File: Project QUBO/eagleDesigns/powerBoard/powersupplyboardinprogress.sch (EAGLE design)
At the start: 8 parts

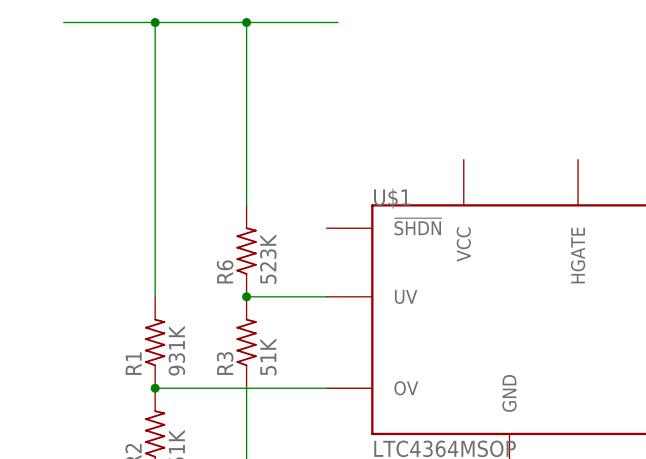
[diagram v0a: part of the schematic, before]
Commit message: Added supporting components for the SHDN pin to the schematic and part's list
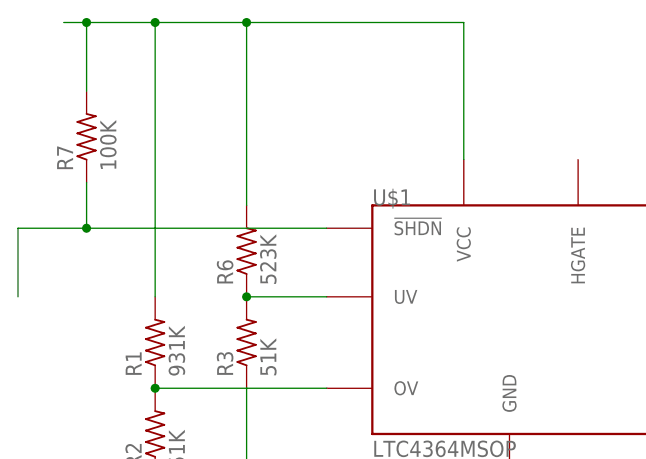
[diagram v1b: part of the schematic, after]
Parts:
- added R7: 100K, resistor:R-US_R0805
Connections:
- new net N$1: R7.1, U$1.!SHDN!
- net N$7: now also R7.2, U$1.VCC
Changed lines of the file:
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@@
 <part name="R3" library="resistor" deviceset="R-US_" device="M0805" value="51K"/>
 <part name="R6" library="resistor" deviceset="R-US_" device="M0805" value="523K"/>
+<part name="R7" library="resistor" deviceset="R-US_" device="R0805" value="100K"/>
 </parts>
 <sheets>
@@
 <instance part="R3" gate="G$1" x="27.94" y="73.66" rot="R90"/>
 <instance part="R6" gate="G$1" x="27.94" y="83.82" rot="R90"/>
+<instance part="R7" gate="G$1" x="10.16" y="96.52" rot="R90"/>
 </instances>
 <busses>
@@
 <net name="N$7" class="0">
 <segment>
-<wire x1="27.94" y1="109.22" x2="38.1" y2="109.22" width="0.1524" layer="91"/>
 <pinref part="R6" gate="G$1" pin="2"/>
 <wire x1="27.94" y1="88.9" x2="27.94" y2="109.22" width="0.1524" layer="91"/>
@@
 <wire x1="17.78" y1="109.22" x2="27.94" y2="109.22" width="0.1524" layer="91"/>
 <junction x="27.94" y="109.22"/>
-<wire x1="7.62" y1="109.22" x2="17.78" y2="109.22" width="0.1524" layer="91"/>
+<wire x1="7.62" y1="109.22" x2="10.16" y2="109.22" width="0.1524" layer="91"/>
 <junction x="17.78" y="109.22"/>
+<pinref part="U$1" gate="G$1" pin="VCC"/>
+<wire x1="10.16" y1="109.22" x2="17.78" y2="109.22" width="0.1524" layer="91"/>
+<wire x1="27.94" y1="109.22" x2="52.07" y2="109.22" width="0.1524" layer="91"/>
+<wire x1="52.07" y1="109.22" x2="52.07" y2="93.98" width="0.1524" layer="91"/>
+<pinref part="R7" gate="G$1" pin="2"/>
+<wire x1="10.16" y1="109.22" x2="10.16" y2="101.6" width="0.1524" layer="91"/>
+<junction x="10.16" y="109.22"/>
 </segment>
 </net>
+<net name="N$1" class="0">
+<segment>
+<pinref part="R7" gate="G$1" pin="1"/>
+<wire x1="10.16" y1="91.44" x2="10.16" y2="86.36" width="0.1524" layer="91"/>
+<pinref part="U$1" gate="G$1" pin="!SHDN!"/>
+<wire x1="10.16" y1="86.36" x2="36.83" y2="86.36" width="0.1524" layer="91"/>
+<wire x1="10.16" y1="86.36" x2="2.54" y2="86.36" width="0.1524" layer="91"/>
+<wire x1="2.54" y1="86.36" x2="2.54" y2="78.74" width="0.1524" layer="91"/>
+<junction x="10.16" y="86.36"/>
+</segment>
+</net>

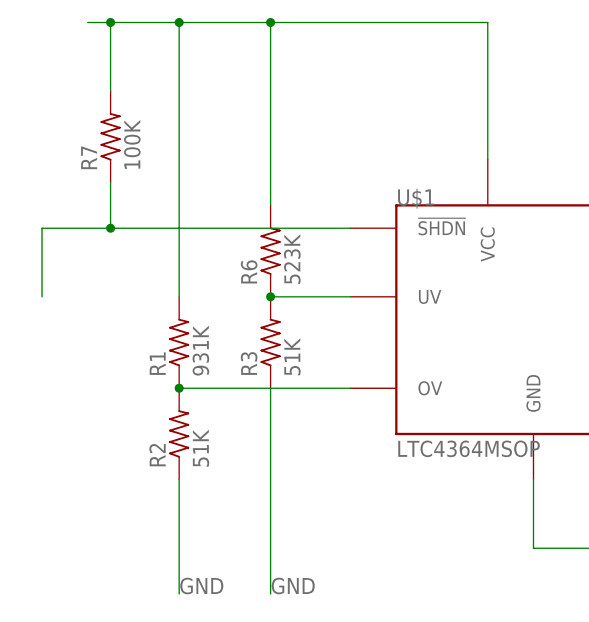
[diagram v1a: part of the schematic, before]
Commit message: 
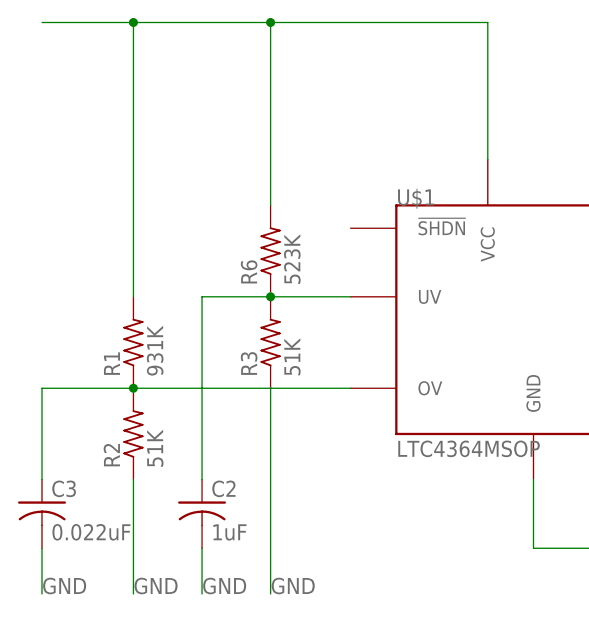
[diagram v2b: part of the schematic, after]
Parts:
- removed R7: 100K, resistor:R-US_R0805
- added C2: 1uF, resistor:C-USC0805
- added C3: 0.022uF, resistor:C-USC0805
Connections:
- removed net N$1: R7.1, U$1.!SHDN!
- net GND: now also C2.2, C3.2
- net N$5: now also C2.1
- net N$6: now also C3.1
- net N$7: no longer R7.2
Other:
- moved on the sheet: R1, R2
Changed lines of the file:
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@@
 <?xml version="1.0" encoding="utf-8"?>
 <!DOCTYPE eagle SYSTEM "eagle.dtd">
-<eagle version="8.3.2">
+<eagle version="8.4.0">
 <drawing>
 <settings>
@@
 <part name="R3" library="resistor" deviceset="R-US_" device="M0805" value="51K"/>
 <part name="R6" library="resistor" deviceset="R-US_" device="M0805" value="523K"/>
-<part name="R7" library="resistor" deviceset="R-US_" device="R0805" value="100K"/>
+<part name="C2" library="resistor" deviceset="C-US" device="C0805" value="1uF"/>
+<part name="C3" library="resistor" deviceset="C-US" device="C0805" value="0.022uF"/>
 </parts>
 <sheets>
@@
 <instance part="R4" gate="G$1" x="119.38" y="76.2" rot="R90"/>
 <instance part="R5" gate="G$1" x="119.38" y="85.09" rot="R90"/>
-<instance part="R1" gate="G$1" x="17.78" y="73.66" rot="R90"/>
-<instance part="R2" gate="G$1" x="17.78" y="63.5" rot="R90"/>
+<instance part="R1" gate="G$1" x="12.7" y="73.66" rot="R90"/>
+<instance part="R2" gate="G$1" x="12.7" y="63.5" rot="R90"/>
 <instance part="R3" gate="G$1" x="27.94" y="73.66" rot="R90"/>
 <instance part="R6" gate="G$1" x="27.94" y="83.82" rot="R90"/>
-<instance part="R7" gate="G$1" x="10.16" y="96.52" rot="R90"/>
+<instance part="C2" gate="G$1" x="20.32" y="55.88"/>
+<instance part="C3" gate="G$1" x="2.54" y="55.88"/>
 </instances>
 <busses>
@@
 <segment>
 <pinref part="R2" gate="G$1" pin="1"/>
-<wire x1="17.78" y1="58.42" x2="17.78" y2="45.72" width="0.1524" layer="91"/>
-<label x="17.78" y="45.72" size="1.778" layer="95"/>
+<wire x1="12.7" y1="58.42" x2="12.7" y2="45.72" width="0.1524" layer="91"/>
+<label x="12.7" y="45.72" size="1.778" layer="95"/>
 </segment>
 <segment>
@@
 <label x="27.94" y="45.72" size="1.778" layer="95"/>
 </segment>
+<segment>
+<pinref part="C2" gate="G$1" pin="2"/>
+<wire x1="20.32" y1="50.8" x2="20.32" y2="45.72" width="0.1524" layer="91"/>
+<label x="20.32" y="45.72" size="1.778" layer="95"/>
+</segment>
+<segment>
+<pinref part="C3" gate="G$1" pin="2"/>
+<wire x1="2.54" y1="50.8" x2="2.54" y2="45.72" width="0.1524" layer="91"/>
+<label x="2.54" y="45.72" size="1.778" layer="95"/>
+</segment>
 </net>
 <net name="N$3" class="0">
@@
 <pinref part="R2" gate="G$1" pin="2"/>
 <pinref part="R1" gate="G$1" pin="1"/>
-<junction x="17.78" y="68.58"/>
+<junction x="12.7" y="68.58"/>
 <pinref part="U$1" gate="G$1" pin="OV"/>
-<wire x1="17.78" y1="68.58" x2="36.83" y2="68.58" width="0.1524" layer="91"/>
+<wire x1="12.7" y1="68.58" x2="36.83" y2="68.58" width="0.1524" layer="91"/>
+<wire x1="12.7" y1="68.58" x2="2.54" y2="68.58" width="0.1524" layer="91"/>
+<wire x1="2.54" y1="68.58" x2="2.54" y2="58.42" width="0.1524" layer="91"/>
+<pinref part="C3" gate="G$1" pin="1"/>
 </segment>
 </net>
@@
 <wire x1="27.94" y1="78.74" x2="36.83" y2="78.74" width="0.1524" layer="91"/>
 <junction x="27.94" y="78.74"/>
+<wire x1="27.94" y1="78.74" x2="20.32" y2="78.74" width="0.1524" layer="91"/>
+<wire x1="20.32" y1="78.74" x2="20.32" y2="58.42" width="0.1524" layer="91"/>
+<pinref part="C2" gate="G$1" pin="1"/>
 </segment>
 </net>
@@
 <wire x1="27.94" y1="88.9" x2="27.94" y2="109.22" width="0.1524" layer="91"/>
 <pinref part="R1" gate="G$1" pin="2"/>
-<wire x1="17.78" y1="78.74" x2="17.78" y2="109.22" width="0.1524" layer="91"/>
-<wire x1="17.78" y1="109.22" x2="27.94" y2="109.22" width="0.1524" layer="91"/>
+<wire x1="12.7" y1="78.74" x2="12.7" y2="109.22" width="0.1524" layer="91"/>
+<wire x1="12.7" y1="109.22" x2="27.94" y2="109.22" width="0.1524" layer="91"/>
 <junction x="27.94" y="109.22"/>
-<wire x1="7.62" y1="109.22" x2="10.16" y2="109.22" width="0.1524" layer="91"/>
-<junction x="17.78" y="109.22"/>
+<junction x="12.7" y="109.22"/>
 <pinref part="U$1" gate="G$1" pin="VCC"/>
-<wire x1="10.16" y1="109.22" x2="17.78" y2="109.22" width="0.1524" layer="91"/>
+<wire x1="2.54" y1="109.22" x2="12.7" y2="109.22" width="0.1524" layer="91"/>
 <wire x1="27.94" y1="109.22" x2="52.07" y2="109.22" width="0.1524" layer="91"/>
 <wire x1="52.07" y1="109.22" x2="52.07" y2="93.98" width="0.1524" layer="91"/>
-<pinref part="R7" gate="G$1" pin="2"/>
-<wire x1="10.16" y1="109.22" x2="10.16" y2="101.6" width="0.1524" layer="91"/>
-<junction x="10.16" y="109.22"/>
-</segment>
-</net>
-<net name="N$1" class="0">
-<segment>
-<pinref part="R7" gate="G$1" pin="1"/>
-<wire x1="10.16" y1="91.44" x2="10.16" y2="86.36" width="0.1524" layer="91"/>
-<pinref part="U$1" gate="G$1" pin="!SHDN!"/>
-<wire x1="10.16" y1="86.36" x2="36.83" y2="86.36" width="0.1524" layer="91"/>
-<wire x1="10.16" y1="86.36" x2="2.54" y2="86.36" width="0.1524" layer="91"/>
-<wire x1="2.54" y1="86.36" x2="2.54" y2="78.74" width="0.1524" layer="91"/>
-<junction x="10.16" y="86.36"/>
-</segment>
-</net>
+</segment>
+</net>

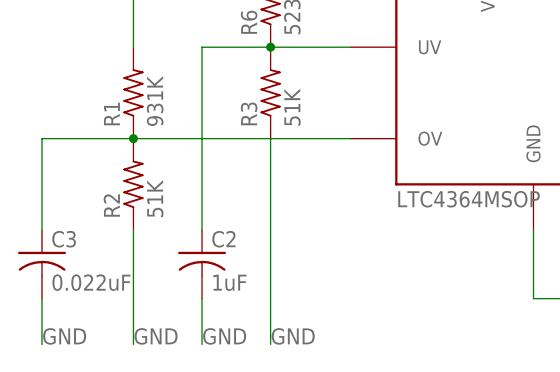
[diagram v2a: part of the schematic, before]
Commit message: 
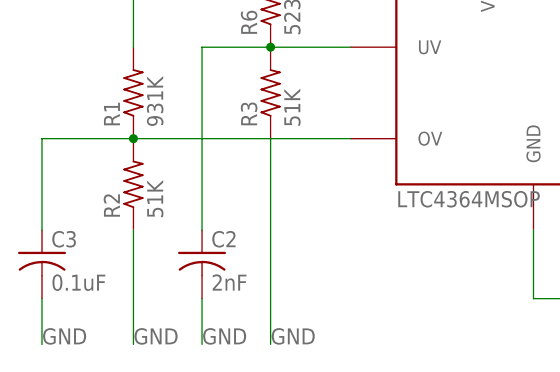
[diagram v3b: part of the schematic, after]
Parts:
- C2: value 1uF -> 2nF
- C3: value 0.022uF -> 0.1uF
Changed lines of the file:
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@@
 <part name="R3" library="resistor" deviceset="R-US_" device="M0805" value="51K"/>
 <part name="R6" library="resistor" deviceset="R-US_" device="M0805" value="523K"/>
-<part name="C2" library="resistor" deviceset="C-US" device="C0805" value="1uF"/>
-<part name="C3" library="resistor" deviceset="C-US" device="C0805" value="0.022uF"/>
+<part name="C2" library="resistor" deviceset="C-US" device="C0805" value="2nF"/>
+<part name="C3" library="resistor" deviceset="C-US" device="C0805" value="0.1uF"/>
 </parts>
 <sheets>

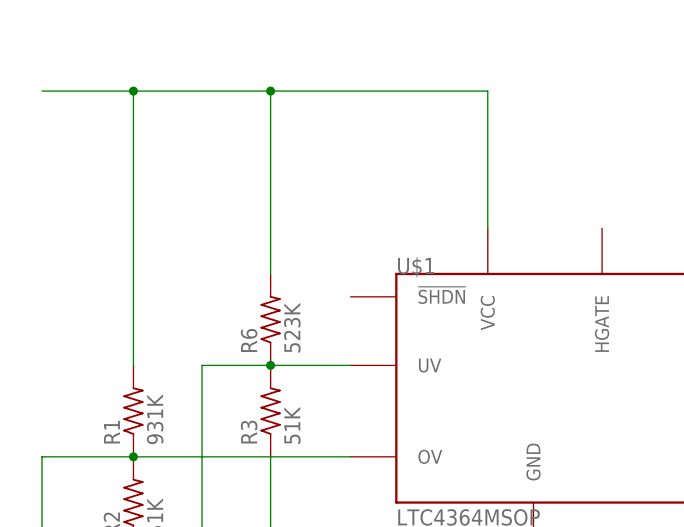
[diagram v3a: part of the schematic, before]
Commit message: Added a description of all the LTC4364 functionality (LTC4364 Notes.txt)
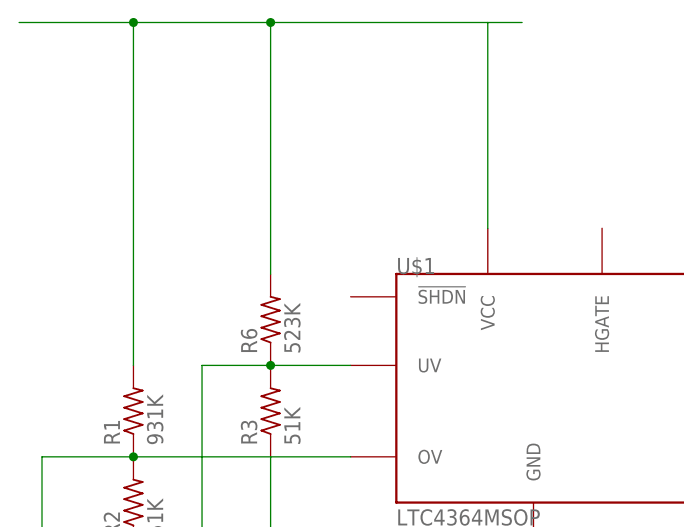
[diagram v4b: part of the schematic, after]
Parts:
- C3: SPICEPREFIX (none) -> C
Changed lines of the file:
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@@
 <part name="R6" library="resistor" deviceset="R-US_" device="M0805" value="523K"/>
 <part name="C2" library="resistor" deviceset="C-US" device="C0805" value="2nF"/>
-<part name="C3" library="resistor" deviceset="C-US" device="C0805" value="0.1uF"/>
+<part name="C3" library="resistor" deviceset="C-US" device="C0805" value="0.1uF">
+<attribute name="SPICEPREFIX" value="C"/>
+</part>
 </parts>
 <sheets>
@@
 <segment>
 <pinref part="R6" gate="G$1" pin="2"/>
-<wire x1="27.94" y1="88.9" x2="27.94" y2="109.22" width="0.1524" layer="91"/>
+<wire x1="27.94" y1="88.9" x2="27.94" y2="116.84" width="0.1524" layer="91"/>
 <pinref part="R1" gate="G$1" pin="2"/>
-<wire x1="12.7" y1="78.74" x2="12.7" y2="109.22" width="0.1524" layer="91"/>
-<wire x1="12.7" y1="109.22" x2="27.94" y2="109.22" width="0.1524" layer="91"/>
-<junction x="27.94" y="109.22"/>
-<junction x="12.7" y="109.22"/>
+<wire x1="12.7" y1="78.74" x2="12.7" y2="116.84" width="0.1524" layer="91"/>
+<wire x1="12.7" y1="116.84" x2="27.94" y2="116.84" width="0.1524" layer="91"/>
+<junction x="27.94" y="116.84"/>
 <pinref part="U$1" gate="G$1" pin="VCC"/>
-<wire x1="2.54" y1="109.22" x2="12.7" y2="109.22" width="0.1524" layer="91"/>
-<wire x1="27.94" y1="109.22" x2="52.07" y2="109.22" width="0.1524" layer="91"/>
-<wire x1="52.07" y1="109.22" x2="52.07" y2="93.98" width="0.1524" layer="91"/>
+<wire x1="27.94" y1="116.84" x2="52.07" y2="116.84" width="0.1524" layer="91"/>
+<wire x1="52.07" y1="116.84" x2="52.07" y2="93.98" width="0.1524" layer="91"/>
+<wire x1="12.7" y1="116.84" x2="0" y2="116.84" width="0.1524" layer="91"/>
+<junction x="12.7" y="116.84"/>
+<wire x1="55.88" y1="116.84" x2="52.07" y2="116.84" width="0.1524" layer="91"/>
 </segment>
 </net>

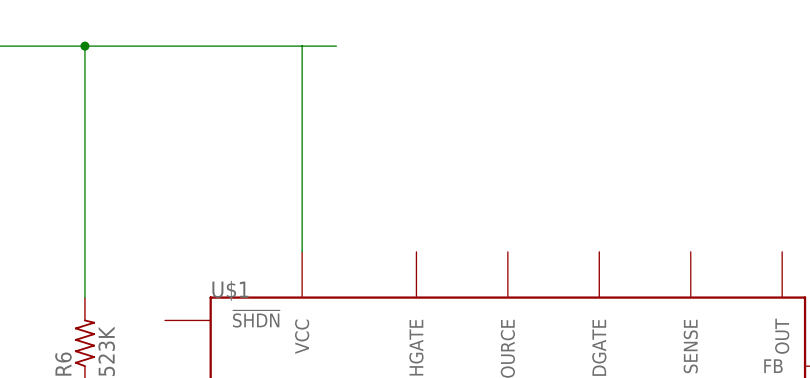
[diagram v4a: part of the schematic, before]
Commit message: Added the IRF7458PbF N-Channel MOSFET SMD Footprint to eagleLibraries
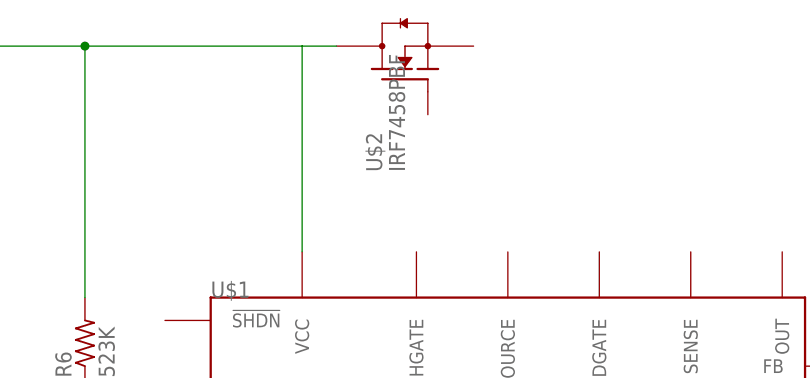
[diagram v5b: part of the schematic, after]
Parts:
- added U$2: IRF7458PBF, transistor-fet:IRF7458PBF
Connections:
- net N$7: now also U$2.D
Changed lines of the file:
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@@
 <?xml version="1.0" encoding="utf-8"?>
 <!DOCTYPE eagle SYSTEM "eagle.dtd">
-<eagle version="8.4.0">
+<eagle version="8.4.1">
 <drawing>
 <settings>
@@
 <attribute name="SPICEPREFIX" value="C"/>
 </part>
+<part name="U$2" library="transistor-fet" deviceset="IRF7458PBF" device=""/>
 </parts>
 <sheets>
@@
 <instance part="C2" gate="G$1" x="20.32" y="55.88"/>
 <instance part="C3" gate="G$1" x="2.54" y="55.88"/>
+<instance part="U$2" gate="G$1" x="63.5" y="114.3" rot="R90"/>
 </instances>
 <busses>
@@
 <junction x="12.7" y="116.84"/>
 <wire x1="55.88" y1="116.84" x2="52.07" y2="116.84" width="0.1524" layer="91"/>
-</segment>
-</net>
+<pinref part="U$2" gate="G$1" pin="D"/>
+</segment>
+</net>
